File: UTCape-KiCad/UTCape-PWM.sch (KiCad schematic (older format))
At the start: 4 parts

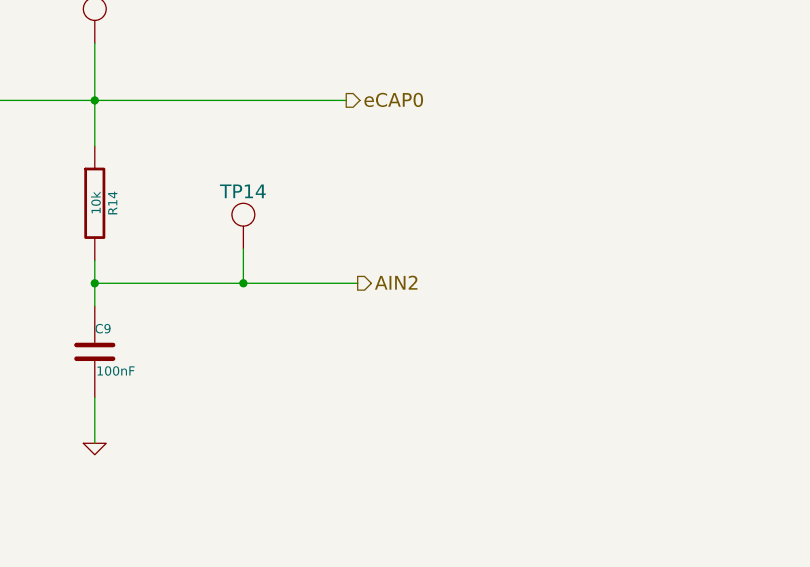
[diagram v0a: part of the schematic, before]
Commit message: layed out PCB, some minor wiring changes for layout
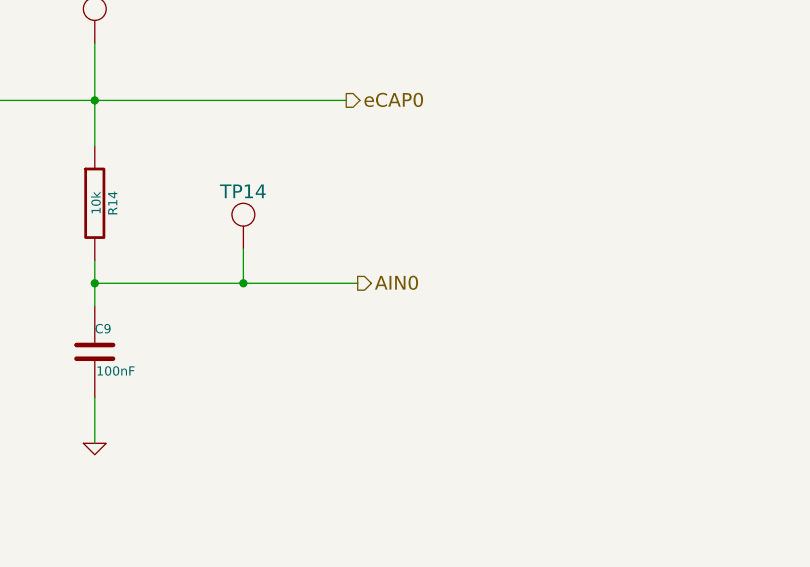
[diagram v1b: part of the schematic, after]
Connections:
- net AIN2 renamed AIN0
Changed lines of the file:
@@
 LIBS:contrib
 LIBS:valves
+LIBS:beagleboneblack
 LIBS:GrayCatLabs
-LIBS:BeagleBoneBlack
 LIBS:UTCape-cache
 EELAYER 27 0
@@
 PWM1A
 Text HLabel 6350 3900 2    60   Output ~ 0
-AIN2
+AIN0
 Text HLabel 6300 3100 2    60   Output ~ 0
 eCAP0
@@
 03 43 83 61 8C 09 03 03 03 03 43 83 61 8C 09 03 03 03 03 43 83 61 8C 09 03 03 03 03 43 83 61 03
 60 D2 64 32 30 30 30 30 34 84 CF 1C 00 A9 00 9C 01 A8 8B 59 19 06 06 06 06 06 E9 E3 33 80 C5 FF
-07 47 25 A5 D2 E9 03 52 D8 00 00 00 00 49 45 4E 44 AE 42 60 82 76 $EndBitmap
+07 47 25 A5 D2 E9 03 52 D8 00 00 00 00 49 45 4E 44 AE 42 60 82 4A $EndBitmap
 EndData
 $EndBitmap

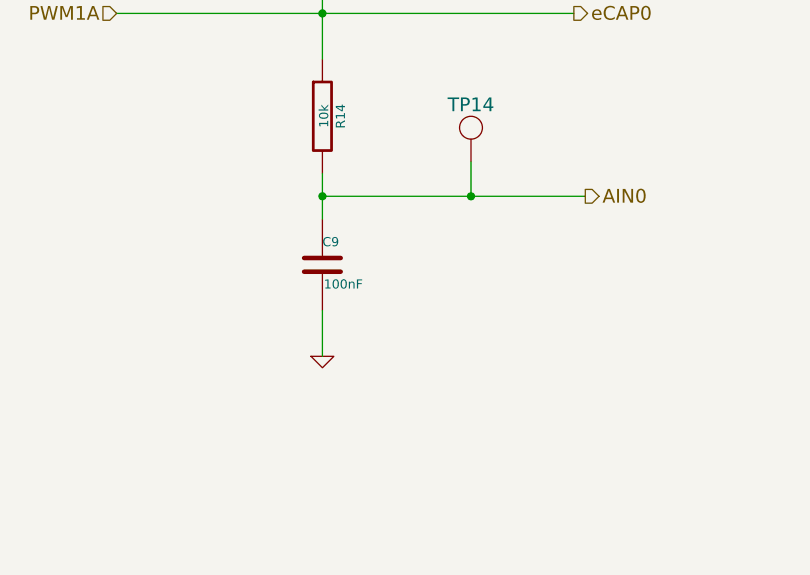
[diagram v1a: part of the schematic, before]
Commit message: added missing resistor in divider plus some protection resistors, regenerated fab files
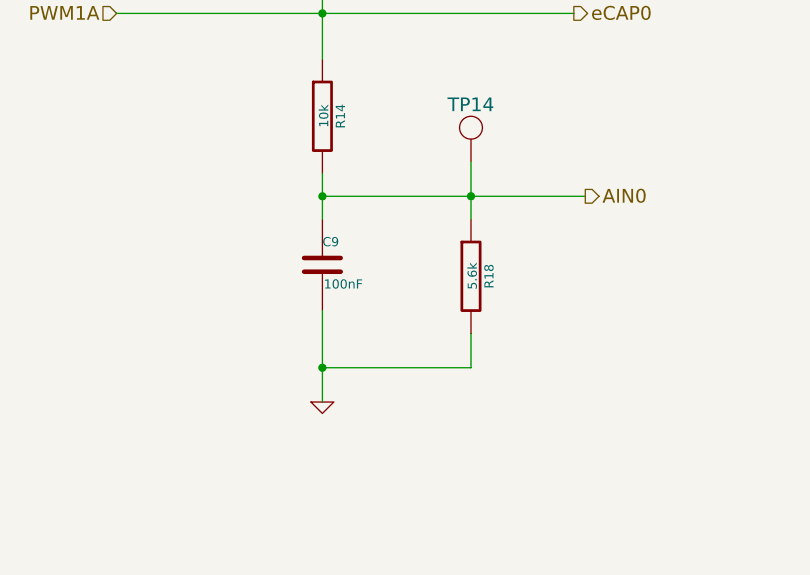
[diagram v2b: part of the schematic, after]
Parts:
- added R18: 5.6k, ~, symbol R
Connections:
- net AIN0: now also R18.1
- net GND: now also R18.2
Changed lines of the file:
@@
 Sheet 7 9
 Title ""
-Date "24 feb 2015"
+Date "24 mar 2015"
 Rev ""
 Comp ""
@@
 L GND #PWR017
 U 1 1 54EEBDAC
-P 5200 4600
-F 0 "#PWR017" H 5200 4600 30  0001 C CNN
-F 1 "GND" H 5200 4530 30  0001 C CNN
-F 2 "" H 5200 4600 60  0000 C CNN
-F 3 "" H 5200 4600 60  0000 C CNN
-	1    5200 4600
+P 5200 4800
+F 0 "#PWR017" H 5200 4800 30  0001 C CNN
+F 1 "GND" H 5200 4730 30  0001 C CNN
+F 2 "" H 5200 4800 60  0000 C CNN
+F 3 "" H 5200 4800 60  0000 C CNN
+	1    5200 4800
 	1    0    0    -1
 $EndComp
@@
 	5200 3900 6350 3900
 Wire Wire Line
-	5850 3900 5850 3750
+	5850 3750 5850 4000
 Connection ~ 5200 3900
 Connection ~ 5850 3900
 Wire Wire Line
-	5200 4400 5200 4600
+	5200 4400 5200 4800
 Text Notes 7350 7550 0    60   ~ 0
 PWM Unit Test Wiring
@@
 03 43 83 61 8C 09 03 03 03 03 43 83 61 8C 09 03 03 03 03 43 83 61 8C 09 03 03 03 03 43 83 61 03
 60 D2 64 32 30 30 30 30 34 84 CF 1C 00 A9 00 9C 01 A8 8B 59 19 06 06 06 06 06 E9 E3 33 80 C5 FF
-07 47 25 A5 D2 E9 03 52 D8 00 00 00 00 49 45 4E 44 AE 42 60 82 4A $EndBitmap
+07 47 25 A5 D2 E9 03 52 D8 00 00 00 00 49 45 4E 44 AE 42 60 82 CF $EndBitmap
 EndData
 $EndBitmap
+$Comp
+L R R18
+U 1 1 54F64156
+P 5850 4250
+F 0 "R18" V 5930 4250 40  0000 C CNN
+F 1 "5.6k" V 5857 4251 40  0000 C CNN
+F 2 "~" V 5780 4250 30  0000 C CNN
+F 3 "~" H 5850 4250 30  0000 C CNN
+	1    5850 4250
+	1    0    0    -1
+$EndComp
+Wire Wire Line
+	5200 4650 5850 4650
+Wire Wire Line
+	5850 4650 5850 4500
+Connection ~ 5200 4650
 $EndSCHEMATC
